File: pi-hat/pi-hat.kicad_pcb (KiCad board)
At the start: 2 copper layers, 65 x 56 mm, 79 parts, among them J1 Conn_01x04_Male, J2 Conn_01x04_Male, J3 Conn_01x05_Male, J4 Conn_01x05_Male, J5 Conn_01x05_Male, J7 Conn_01x07_Male, J8 Conn_01x07_Male, P1 Conn_02x20_Odd_Even, Q1 BSS138, Q10 AO 3415A, Q11 BC 818-25, Q12 BSS138, Q13 BSS138, Q14 BSS138, Q15 BSS138, Q16 BSS138, Q17 AO 3415A, Q2 BSS138, Q3 BSS138, Q4 BC 807-25, Q5 AO 3415A, Q6 BC 807-25, Q7 BC 818-25, Q8 BC 818-25, Q9 BC 818-25, U1 M24C02-WMN

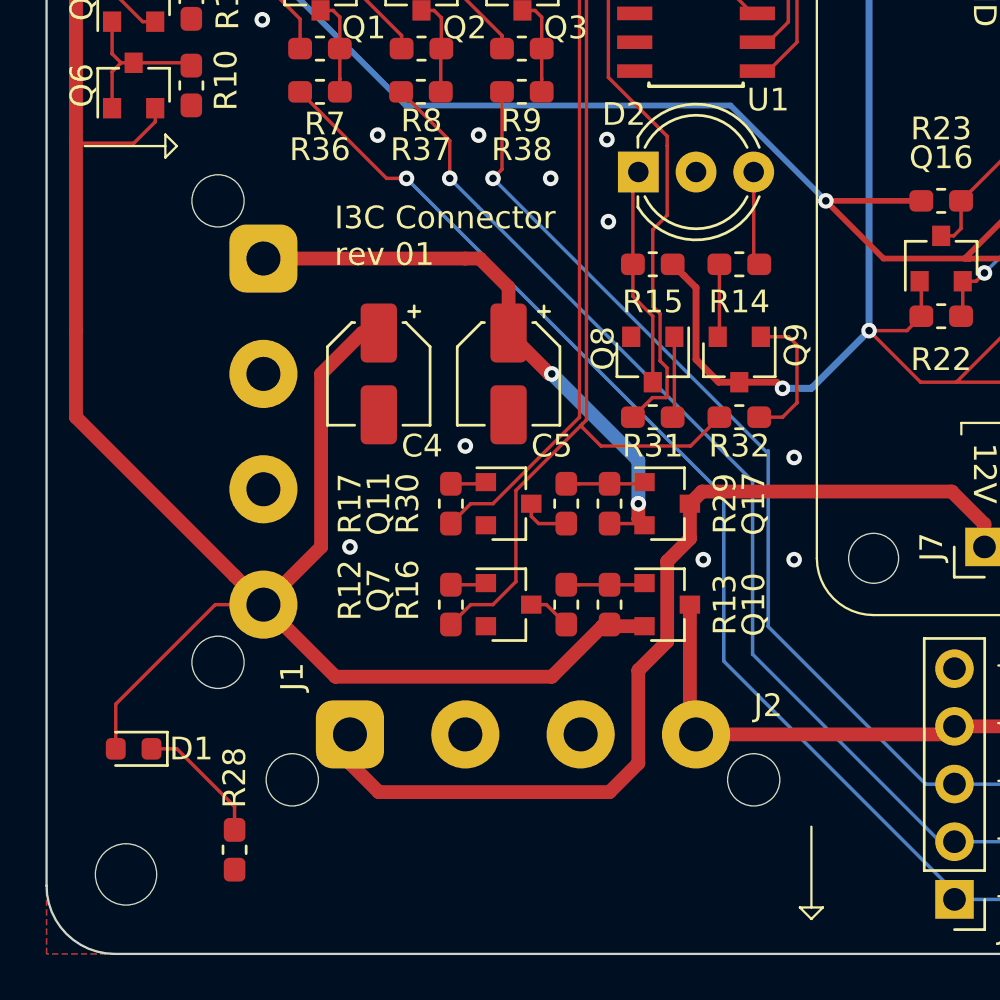
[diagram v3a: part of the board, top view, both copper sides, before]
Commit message: Ground management and max rating for output
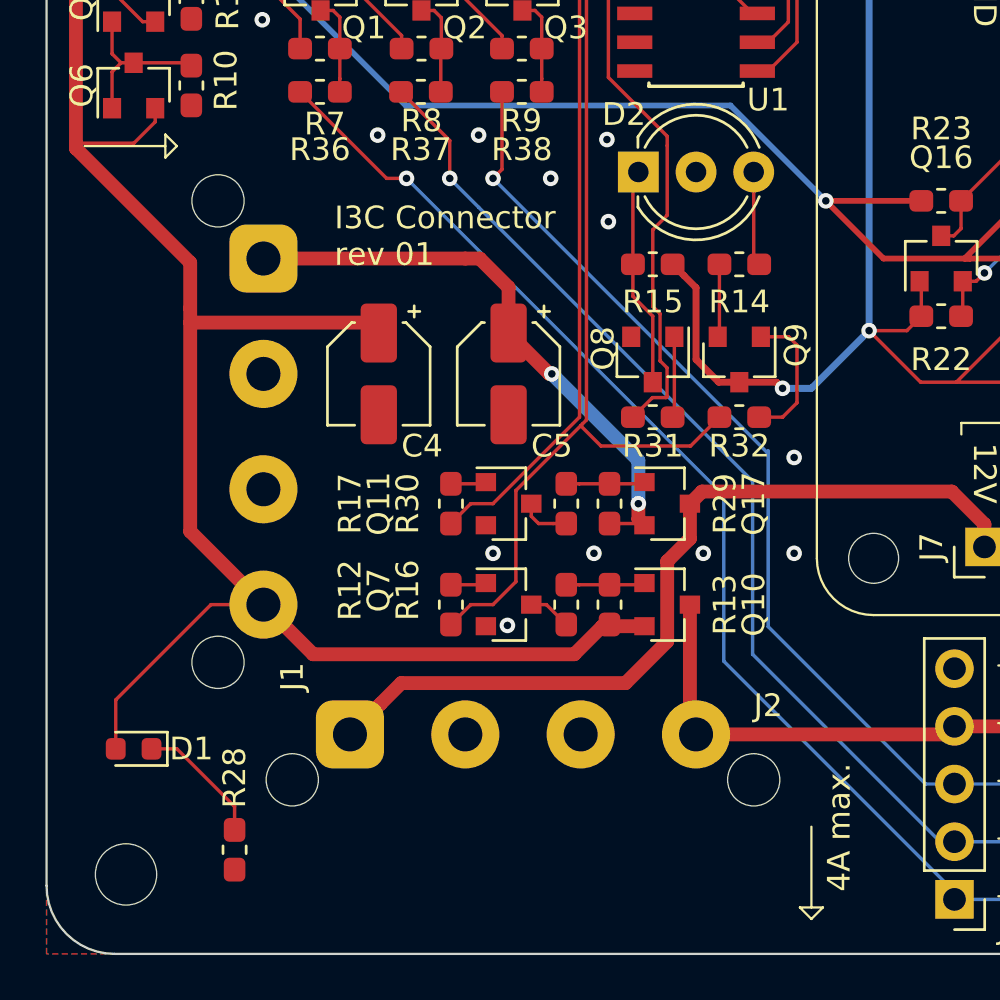
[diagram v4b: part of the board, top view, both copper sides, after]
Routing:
- net +5VP: track 85.2 -> 78.5 mm
- net +12VA: track 42.2 -> 36.9 mm
- net GND: vias 23 -> 24
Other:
- board text added: "4A max."

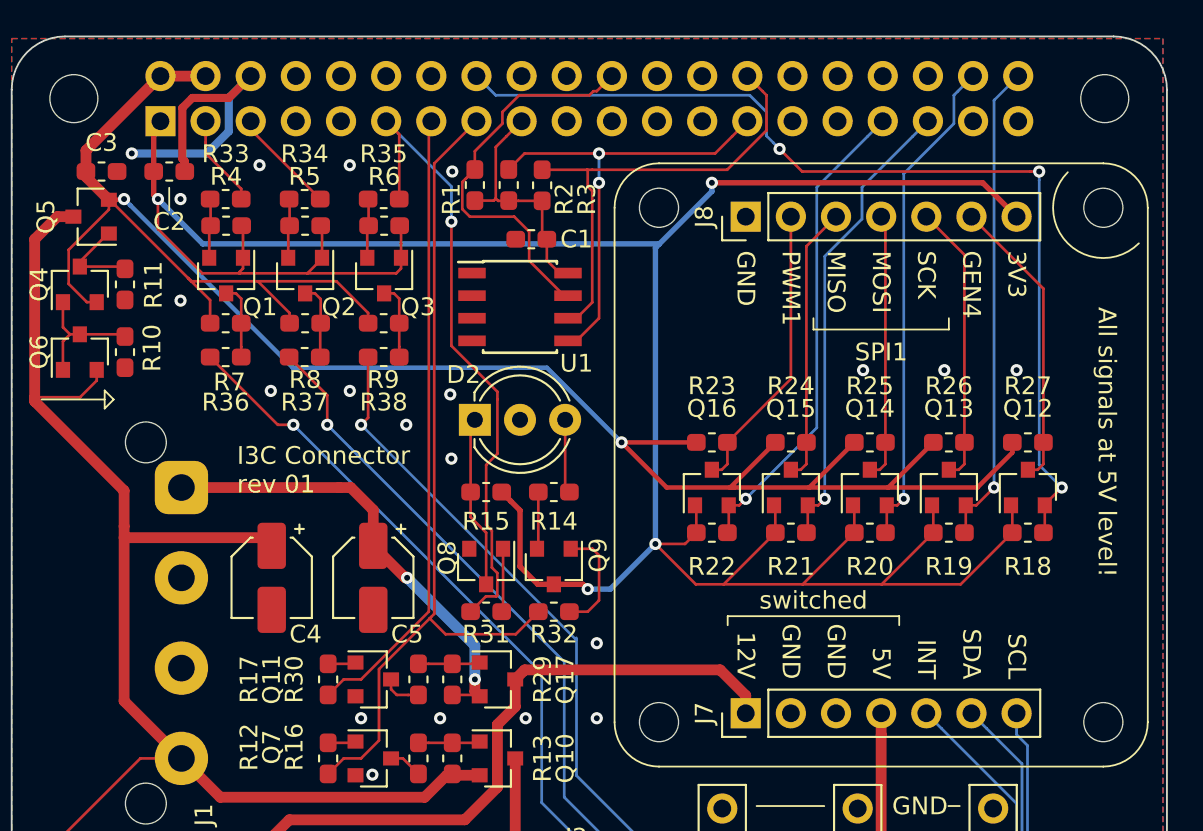
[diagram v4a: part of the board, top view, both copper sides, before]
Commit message: Remove some level shifters
The level shifters made only sense for I3C - removed the rest.
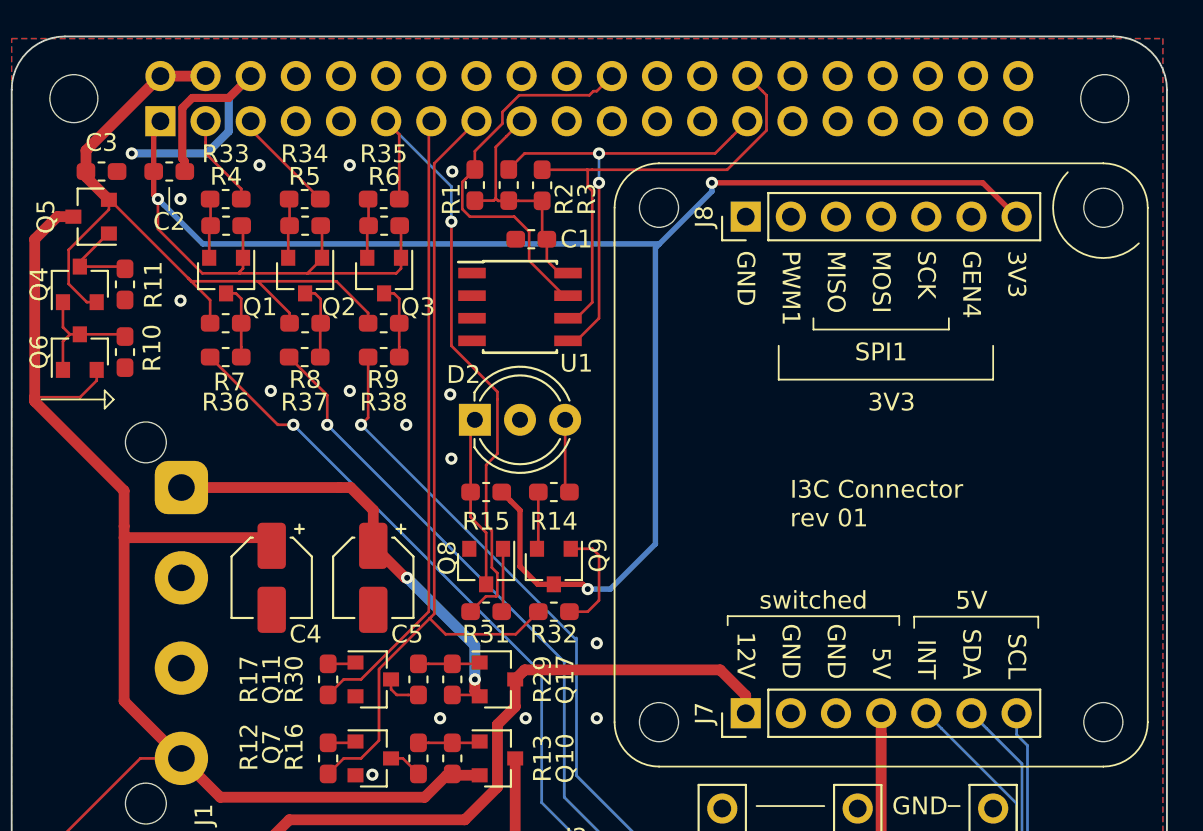
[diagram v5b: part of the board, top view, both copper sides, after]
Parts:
- removed Q12, Q13, Q14, Q15, Q16: BSS138, Package_TO_SOT_SMD:SOT-23
- removed R18, R19, R20, R21, R22, R23, R24, R25, R26, R27: 10K, Capacitor_SMD:C_0603_1608Metric_Pad1.05x0.95mm_HandSolder
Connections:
- J8 pad 2: PWM_5V -> (no net)
- J8 pad 3: SPI_MISO_5V -> (no net)
- J8 pad 4: SPI_MOSI_5V -> (no net)
- J8 pad 5: SPI_SCK_5V -> (no net)
- J8 pad 6: GPIO_5V -> (no net)
- P1 pad 16: GPIO -> (no net)
- P1 pad 33: PWM -> (no net)
- P1 pad 35: SPI_MISO -> (no net)
- P1 pad 38: SPI_MOSI -> (no net)
- P1 pad 40: SPI_SCK -> (no net)
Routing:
- net +5V: track 117.6 -> 43.4 mm, vias 2 -> 0
- net GPIO: track 55.9 -> 0.00 mm, vias 3 -> 0
- net +3V3: track 158.1 -> 113.2 mm, vias 4 -> 3
- net SPI_MOSI: track 28.1 -> 0.00 mm, vias 1 -> 0
- net SPI_SCK: track 27.3 -> 0.00 mm, vias 1 -> 0
- net PWM: track 27.1 -> 0.00 mm, vias 1 -> 0
- net SPI_MISO: track 26.3 -> 0.00 mm, vias 1 -> 0
- net GPIO_5V: track 16.6 -> 0.00 mm
- net PWM_5V: track 16.4 -> 0.00 mm
- net SPI_SCK_5V: track 15.8 -> 0.00 mm
- net SPI_MISO_5V: track 15.6 -> 0.00 mm
- net SPI_MOSI_5V: track 15.0 -> 0.00 mm
- net GND: vias 24 -> 20
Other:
- board text removed: "All signals at 5V level!"

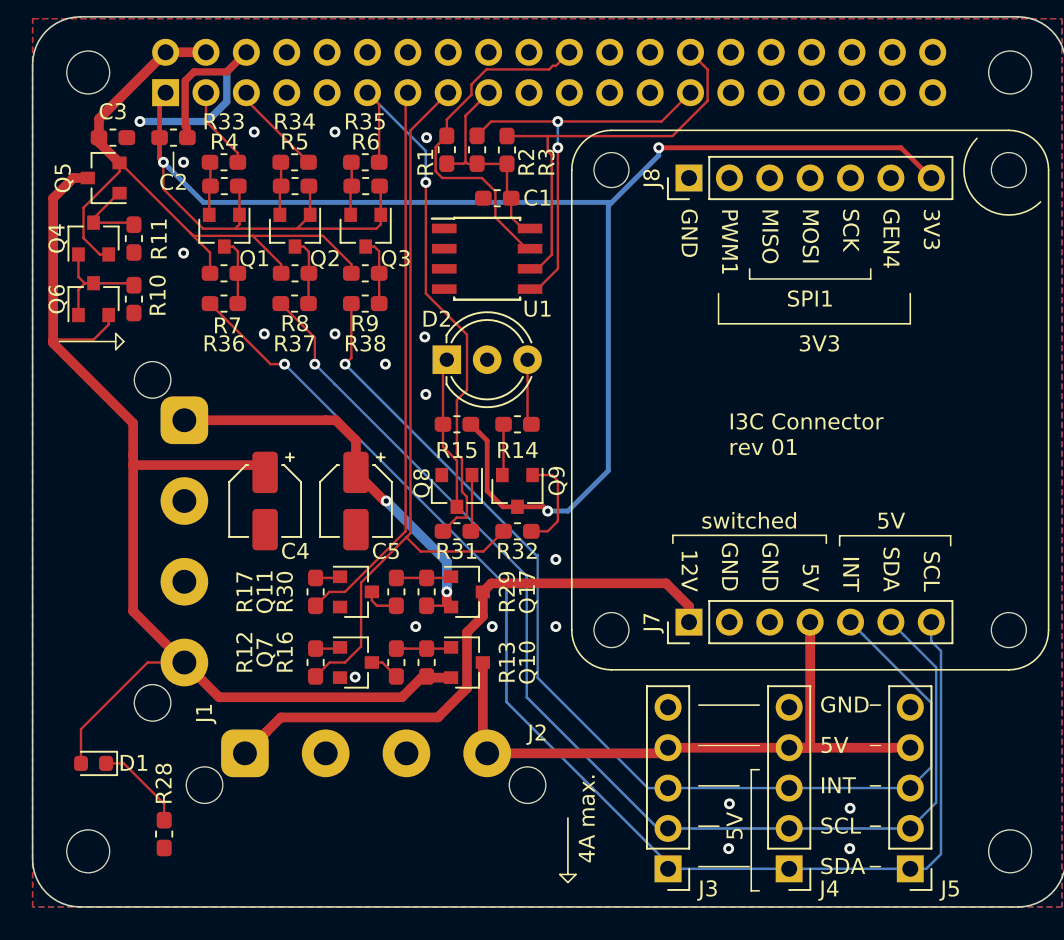
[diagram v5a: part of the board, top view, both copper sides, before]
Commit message: Run RenumKicadPCB to sort designators
https://github.com/penguineer/RenumKicadPCB
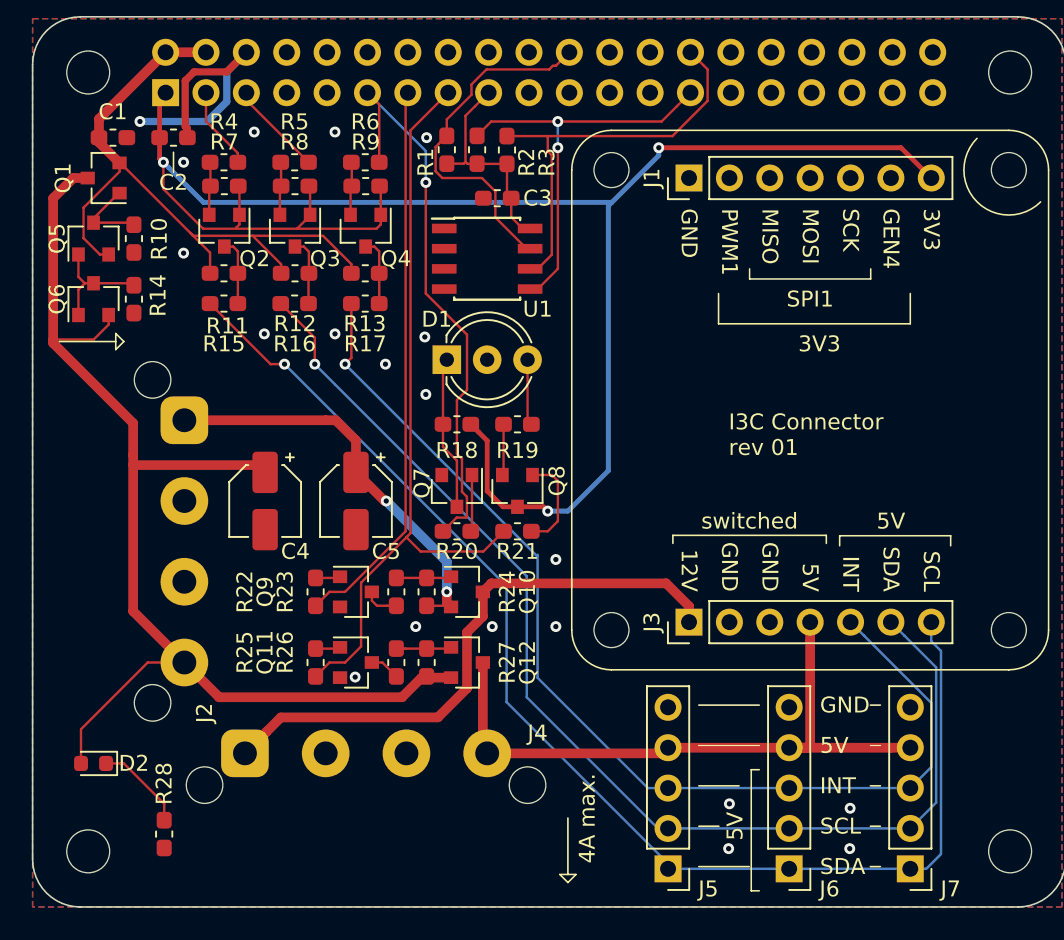
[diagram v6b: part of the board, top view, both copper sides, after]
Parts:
- renumbered C3 to C1, C1 to C3, D2 to D1, D1 to D2, J8 to J1, J1 to J2, J7 to J3, J2 to J4, J3 to J5, J4 to J6, J5 to J7, MK5 to MK3, MK7 to MK4, MK6 to MK5, MK8 to MK6, MK3 to MK7, MK4 to MK8, Q5 to Q1, Q17 to Q10, Q7 to Q11, Q10 to Q12, Q1 to Q2, Q2 to Q3, Q3 to Q4, Q4 to Q5, Q8 to Q7, Q9 to Q8, Q11 to Q9, R11 to R10, R7 to R11, R8 to R12, R9 to R13, R10 to R14, R36 to R15, R37 to R16, R38 to R17, R15 to R18, R14 to R19, R31 to R20, R32 to R21, R17 to R22, R30 to R23, R29 to R24, R12 to R25, R16 to R26, R13 to R27, R33 to R4, R34 to R5, R35 to R6, R4 to R7, R5 to R8, R6 to R9
